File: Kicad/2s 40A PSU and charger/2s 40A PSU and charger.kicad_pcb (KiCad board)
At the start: 4 copper layers, 45 x 20 mm, 109 parts, among them J1 Keystone 3579, J10 USB_C_Receptacle_USB2.0_16P, J11 1.27mm 4 pin socket, J12 USB, J2 JST XH-S Balance Plug, J3 Keystone 3579, J4 Keystone 3569, J5 Keystone 3569, J6 Keystone 3579, J7 Keystone 3579, J8 Keystone 3569, J9 Keystone 3569, Q1 PJA3430, Q2 PJA3430, Q3 Vishay sir404dp, or SiR500DP, Q4 PJA3430, Q5 PJA3430, Q6 Vishay sir404dp, or SiR500DP, U1 BQ76905RGRR, U2 AP63203WU, U3 BQ24780SRUYR, U5 THVD1420DRLR, U6 CH32X035G8U6, U7 TPS7A2633DRV

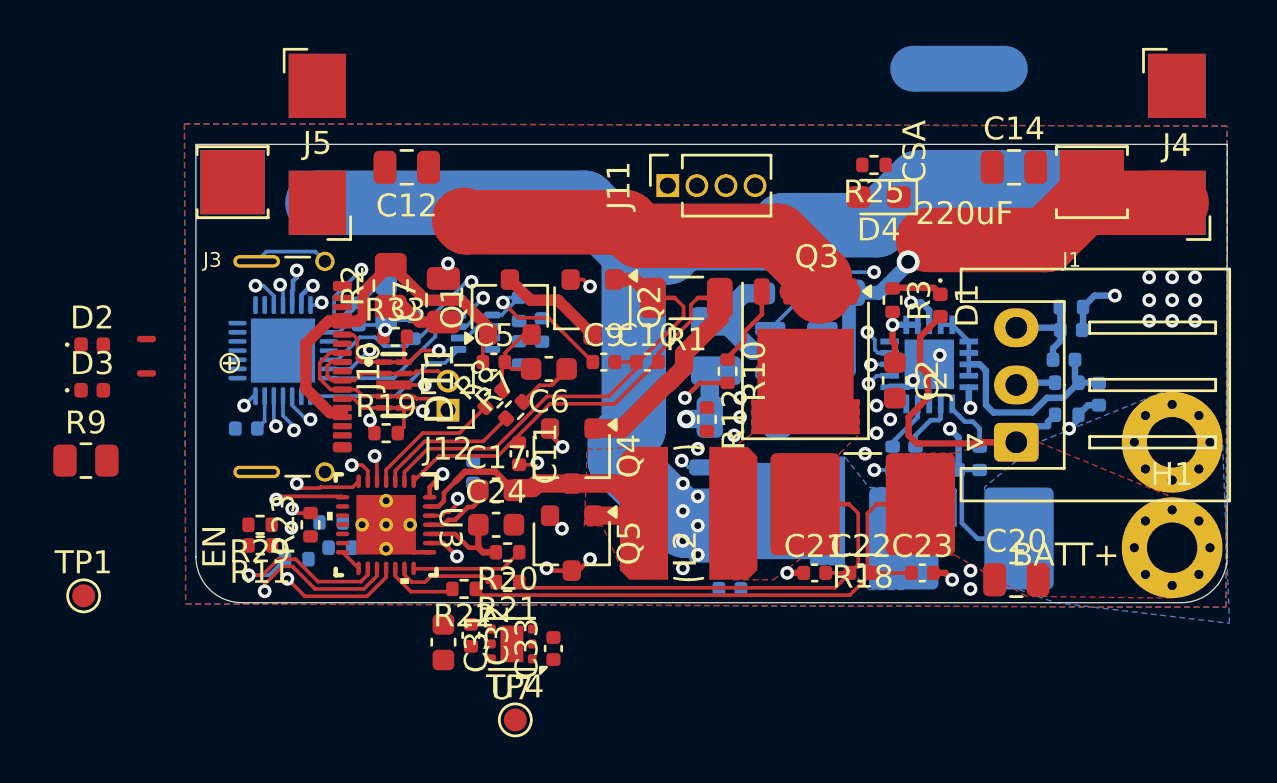
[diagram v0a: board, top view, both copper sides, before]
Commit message: Finished Layout of PSU
Gosh, this has taken a long time on and off, almost 2 months!
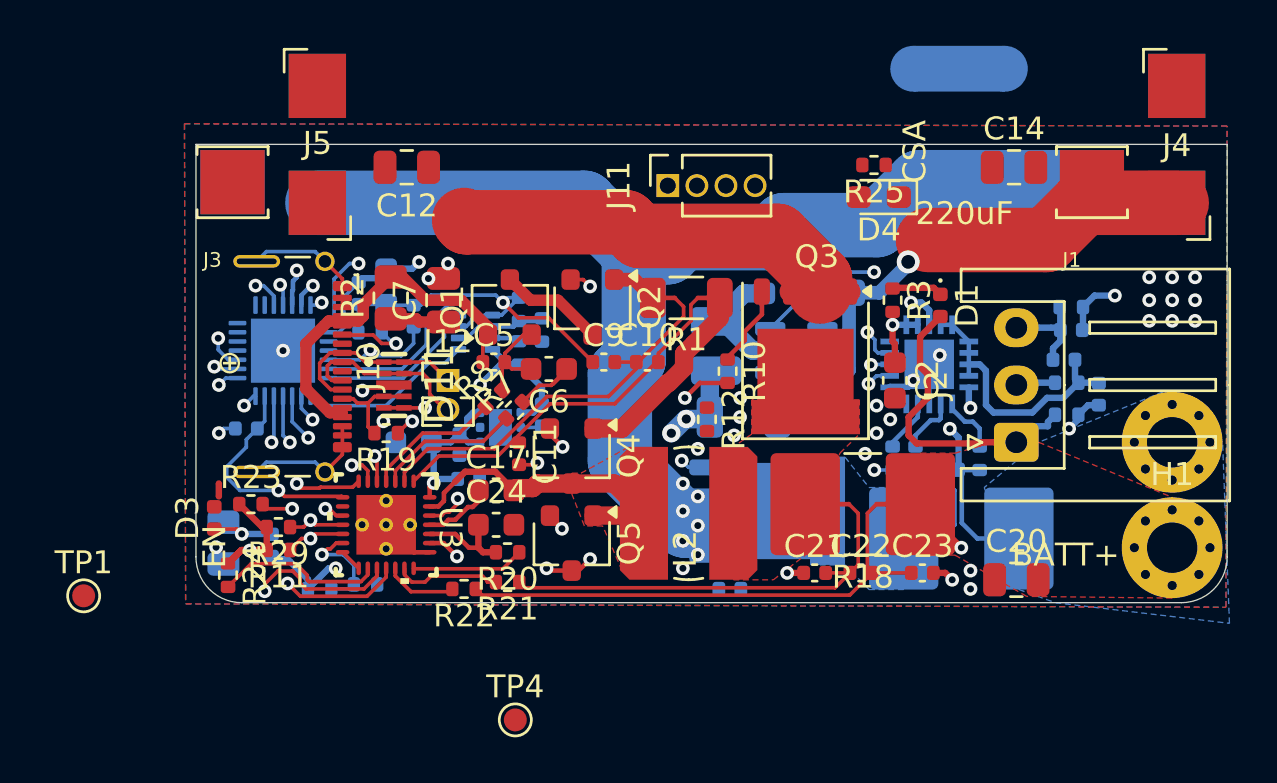
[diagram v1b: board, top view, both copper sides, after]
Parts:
- C31, C32, C33, D2, NT10, R33, R9, U7: moved to B.Cu
- J10: value USB_C_Receptacle_USB2.0_16P -> G-Switch-GT-USB-7025
- R24: moved to F.Cu
- moved NT10 11.8 mm to (112.4, 130.4), turned to -45 degrees
- moved D2 11.7 mm to (111.4, 129.5), turned to -90 degrees
- moved C33 10.2 mm to (123.2, 123.8), turned to -90 degrees
- moved U7 9.46 mm to (121.4, 124.3)
- moved C31 8.82 mm to (117.6, 125.0), turned to 180 degrees
- moved C32 8.34 mm to (119.6, 125.1)
- moved D3 7.71 mm to (108.9, 128.3), turned to 90 degrees
- moved R9 7.00 mm to (109.3, 129.4), turned to 90 degrees
- moved NT12 5.99 mm to (109.1, 127.1), turned to 90 degrees
- moved R24 3.08 mm to (109.5, 130.8), turned to -90 degrees
- moved R30 2.94 mm to (113.5, 131.4)
- moved R23 2.75 mm to (110.5, 127.7), turned to 0 degrees
- moved R31 1.94 mm to (115.5, 131.2)
- moved J12 1.30 mm to (119.1, 122.3), turned to 0 degrees
- moved R33 1.12 mm to (115.7, 120.2)
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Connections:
- D11 pad 1: /Connectors/CC1 -> /Connectors/D+
- D11 pad 10: /Connectors/CC1 -> /Connectors/D+
- D11 pad 4: /Connectors/D+ -> /Connectors/CC2
- D11 pad 5: /Connectors/CC2 -> /Connectors/CC1
- D11 pad 6: /Connectors/CC2 -> /Connectors/CC1
- D11 pad 7: /Connectors/D+ -> /Connectors/CC2
- NT12 pad 2: /Battery Charger/MOTORPWR -> /Battery Charger/IN
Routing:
- net GND: track 19.6 -> 35.5 mm, vias 7 -> 8
- net /Battery Charger/MCU3.3v: track 3.64 -> 18.4 mm, vias 0 -> 3
- net /Battery Charger/Always On PWR: track 1.25 -> 8.40 mm, vias 1 -> 2
- net /Battery Balancer/+BAT: track 0.00 -> 5.19 mm, vias 0 -> 2
- net /MCU/UART1-RTS: track 4.03 -> 9.21 mm, vias 2 -> 0
- net /Battery Charger/Charger IDCHG: track 4.52 -> 9.64 mm
- net Net-(U3-CMPIN): track 0.00 -> 4.58 mm, vias 0 -> 1
- net /Battery Charger/Charger IADP: track 11.1 -> 7.84 mm
- net Net-(D2-K): track 0.00 -> 2.60 mm, vias 0 -> 1
- net /SCL: track 2.45 -> 5.03 mm, vias 2 -> 3
- net /SDA: track 1.77 -> 4.26 mm, vias 2 -> 3
- net /Connectors/RS485-: track 0.00 -> 2.31 mm
- net /Connectors/RS485+: track 0.00 -> 2.23 mm
- net /Connectors/3.3v: track 8.03 -> 9.88 mm, vias 2 -> 3
- net /Battery Charger/Charger PROCHOT: track 0.00 -> 1.82 mm, vias 0 -> 2
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
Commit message: Updated 3v3 psu traces and capacitor position
I rotated the input capacitor to make a more compact shape, and I played around with some of the trace thicknesses
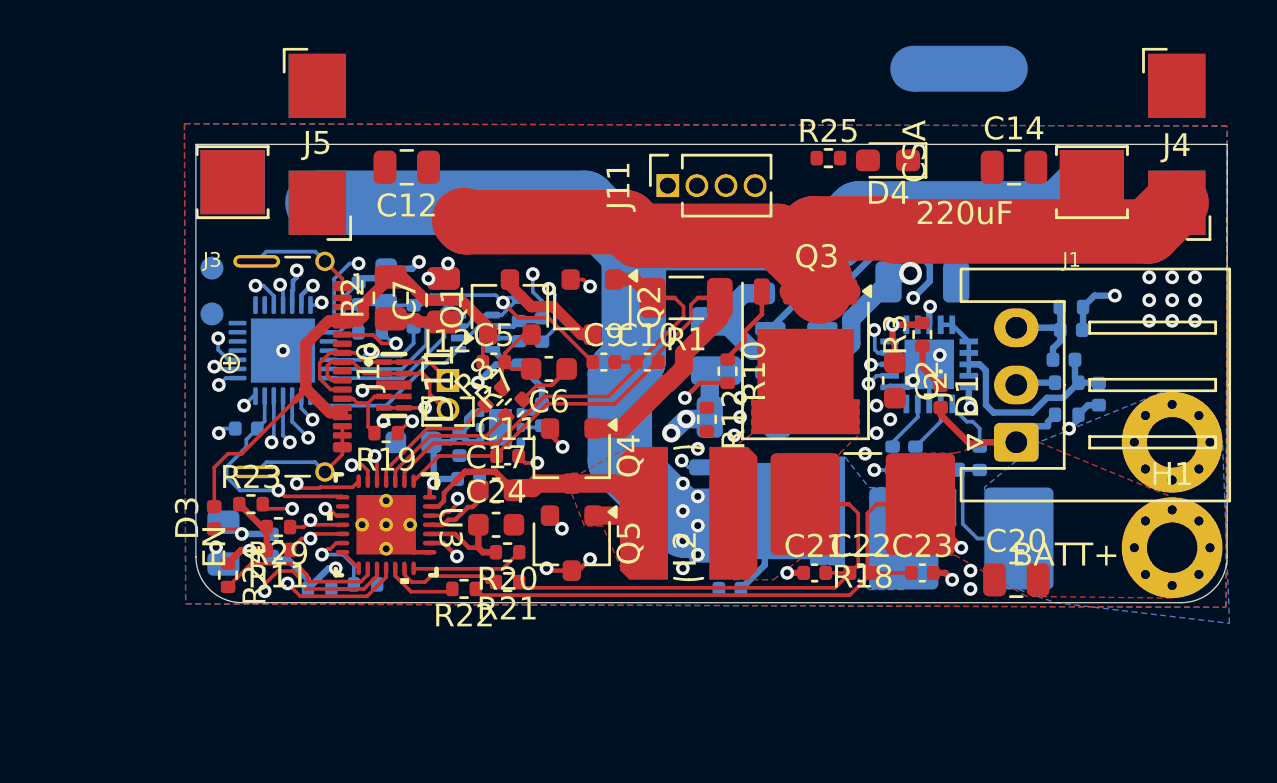
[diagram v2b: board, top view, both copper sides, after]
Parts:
- TP1, TP4: moved to B.Cu
- moved TP4 23.7 mm to (108.8, 117.4), turned to 180 degrees
- moved TP1 13.5 mm to (108.8, 119.4), turned to 180 degrees
- moved NT12 5.38 mm to (112.6, 123.0), turned to 45 degrees
- moved D1 3.97 mm to (140.6, 123.0)
- moved C28 3.54 mm to (139.8, 118.0), turned to 0 degrees
- moved R25 2.01 mm to (135.7, 112.6), turned to 0 degrees
- moved R3 1.98 mm to (139.8, 120.3), turned to 90 degrees
- moved D4 1.65 mm to (138.3, 112.7)
- moved C11 0.51 mm to (121.7, 125.6), turned to 0 degrees
- moved R7 0.10 mm to (122.0, 123.5)
- moved R8 0.10 mm to (121.1, 123.0)
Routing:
- net /Battery Charger/MOTORPWR: track 40.6 -> 50.0 mm
- net Net-(D1-A): track 9.37 -> 2.62 mm
- net Net-(D3-A): track 0.00 -> 6.42 mm
- net Net-(Q6-S): track 5.99 -> 9.82 mm
- net /Connectors/3.3v: track 9.88 -> 13.6 mm
- net Net-(Q1-G): track 8.82 -> 5.32 mm
- net /Connectors/RS485+: track 2.23 -> 4.88 mm, vias 0 -> 1
- net /Connectors/RS485-: track 2.31 -> 4.40 mm, vias 0 -> 1
- net /Battery Balancer/-BAT: track 29.5 -> 27.5 mm, vias 3 -> 2
- net /Battery Balancer/Up: track 17.6 -> 16.2 mm
- net Net-(U1-BAT): track 3.36 -> 4.13 mm

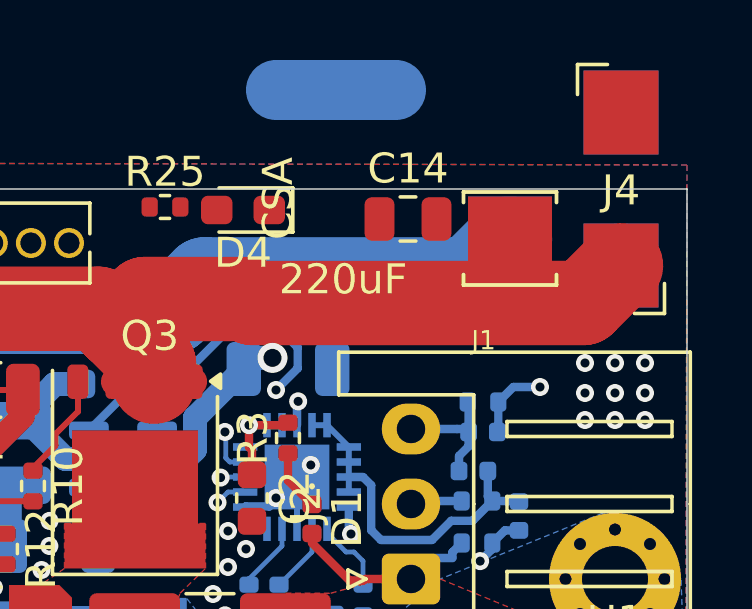
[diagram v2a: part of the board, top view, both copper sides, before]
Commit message: Combined separate ground planes
I now have one solid ground plane. There really was no point in having separate ground planes EXCEPT for keeping the high current return path away from the MCU and sense lines. I have added a keepout zone on the top half, to split to keep the high current return from going into the MCU section, but that is it.
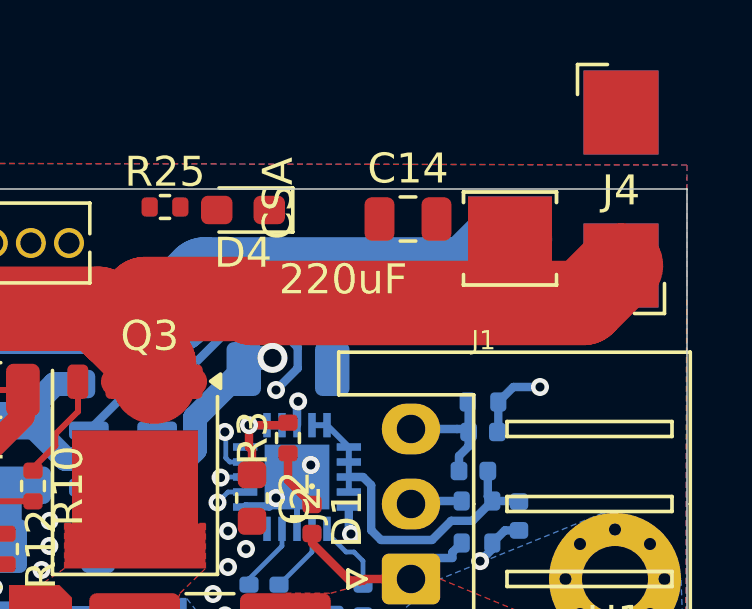
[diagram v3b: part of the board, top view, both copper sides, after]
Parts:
- removed NT1: Main GND NetTie, NetTie:NetTie-2_SMD_Pad2.0mm
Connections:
- C12 pad 1: GNDPWR -> GND
- C14 pad 1: GNDPWR -> GND
- C2 pad 2: GNDPWR -> /Battery Balancer/-BAT
- C20 pad 1: GNDPWR -> GND
- C24 pad 2: GNDPWR -> GND
- C28 pad 2: GNDPWR -> GND
- C31 pad 2: GNDPWR -> GND
- C32 pad 2: GNDPWR -> GND
- C4 pad 2: GNDPWR -> GND
- C7 pad 2: GNDPWR -> GND
- J6 pad 1: GNDPWR -> GND
- J7 pad 1: GNDPWR -> GND
- J8 pad 1: GNDPWR -> GND
- J9 pad 1: GNDPWR -> GND
- Q5 pad 3: GNDPWR -> GND
- Q6 pad 1: GNDPWR -> GND
- Q6 pad 2: GNDPWR -> GND
- Q6 pad 3: GNDPWR -> GND
- R31 pad 1: GNDPWR -> GND
- U2 pad 4: GNDPWR -> GND
- U3 pad 22: GNDPWR -> GND
- U3 pad 29: GNDPWR -> GND
- U7 pad 5: GNDPWR -> GND
- U7 pad 7: GNDPWR -> GND
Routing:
- net GNDPWR: track 55.3 -> 0.00 mm, vias 29 -> 0
- net GND: track 35.6 -> 90.9 mm, vias 8 -> 28
- added copper zone on B.Cu, net GND
- added copper zone on F.Cu, net GND
- added copper zone on In1.Cu, net GND
- added copper zone on In2.Cu, net GND
- removed copper zone on B.Cu, net GNDPWR
- removed copper zone on F.Cu, net GNDPWR
- removed copper zone on In1.Cu, net GNDPWR
- removed copper zone on In2.Cu, net GNDPWR

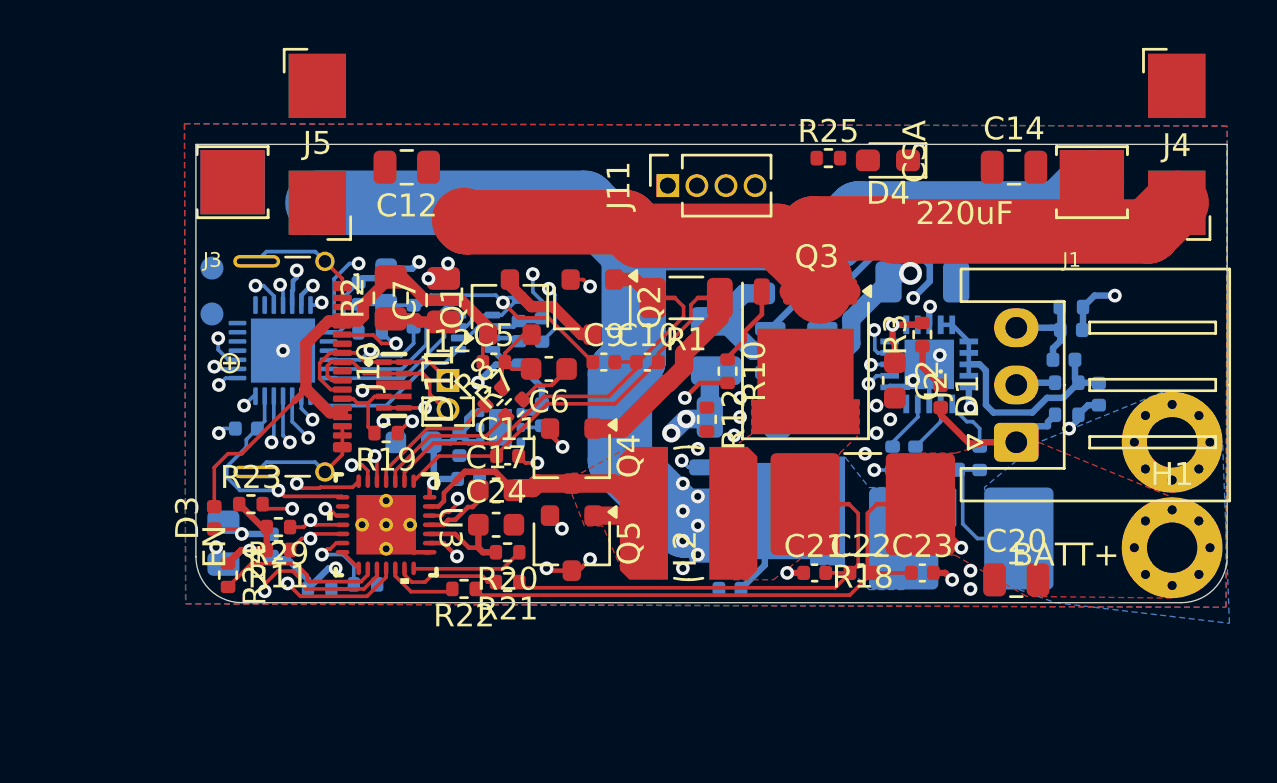
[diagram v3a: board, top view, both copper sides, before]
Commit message: Finished routing PSU
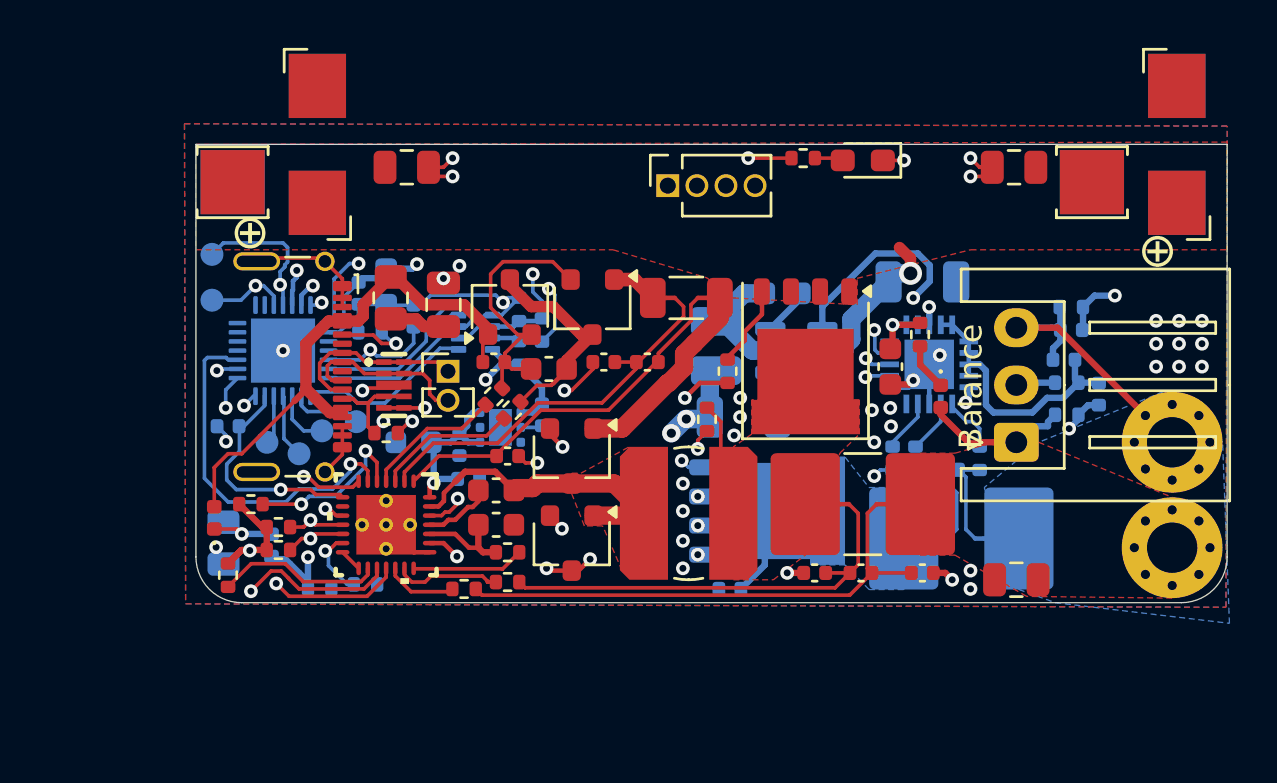
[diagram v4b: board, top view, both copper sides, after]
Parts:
- added NT1: Sense NetTie, custom_Connector:NetTie-2_SMD_Pad0.2mm, B.Cu at (142.3, 129.2)
- added NT11: Sense NetTie, custom_Connector:NetTie-2_SMD_Pad0.2mm, B.Cu at (140.7, 129.2)
- added TP2: CS, TestPoint:TestPoint_Pad_D1.0mm, B.Cu at (115.1, 124.1)
- added TP3: SCK, TestPoint:TestPoint_Pad_D1.0mm, B.Cu at (113.6, 124.5)
- added TP5: SDI, TestPoint:TestPoint_Pad_D1.0mm, B.Cu at (112.6, 125.5)
- added TP6: SDO, TestPoint:TestPoint_Pad_D1.0mm, B.Cu at (111.2, 125.0)
- J10: footprint Connector_USB:USB_C_Receptacle_G-Switch_GT-USB-7025 -> custom_Connector:USB_C_G-Switch_GT-USB-7025-JLCPCBv
- moved D4 1.10 mm to (137.2, 112.7)
- moved R25 1.10 mm to (134.6, 112.6)
- moved C30 0.81 mm to (109.5, 124.3)
- moved C2 0.63 mm to (138.4, 121.7)
- moved TP1 0.60 mm to (108.8, 118.8)
- moved TP4 0.60 mm to (108.8, 116.8)
- moved J12 0.40 mm to (119.1, 121.9)
- moved C7 0.20 mm to (118.9, 119.0)
- moved R7 0.14 mm to (121.9, 123.6)
- moved R3 0.10 mm to (139.7, 120.3)
- moved NT10 0.10 mm to (112.4, 130.5)
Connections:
- C3 pad 1: /Battery Balancer/-BAT -> Net-(C3-Pad1)
- C3 pad 2: Net-(Q6-S) -> Net-(C3-Pad2)
- R4 pad 2: /Battery Balancer/-BAT -> Net-(C3-Pad1)
- R5 pad 2: Net-(Q6-S) -> Net-(C3-Pad2)
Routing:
- net /Connectors/3.3v: track 13.6 -> 63.6 mm
- net /SDA: track 4.26 -> 51.7 mm
- net /SCL: track 5.03 -> 49.8 mm
- net GND: track 90.9 -> 48.1 mm, vias 28 -> 43
- net /Battery Charger/MOTORPWR: track 50.0 -> 8.54 mm
- net /Battery Balancer/+BAT: track 5.19 -> 39.8 mm, vias 2 -> 1
- net /Battery Balancer/Balancer Alert: track 2.25 -> 35.3 mm
- net /MCU/LED: track 1.05 -> 32.5 mm, vias 1 -> 2
- net /Battery Charger/MCU3.3v: track 18.5 -> 43.8 mm
- net /Connectors/CC1: track 5.65 -> 21.8 mm
- net /Connectors/RS485-: track 4.40 -> 18.6 mm
- net /Connectors/CC2: track 8.36 -> 22.3 mm
- net /Connectors/RS485+: track 4.88 -> 18.5 mm
- net /Battery Charger/Always On PWR: track 8.40 -> 21.9 mm
- net /Connectors/D+: track 9.25 -> 22.7 mm
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- added copper zone on F.Cu, net /Battery Charger/MOTORPWR
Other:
- board text added: "+ D+D- -"
- board text added: "BAT+"
- board text added: "BAT-"
- board text added: "Balance"
- board text added: "SWC , SWD"
- board text added: "©2024 Asher Edwards"
- board text removed: "220uF"
- board text removed: "BATT+"
- board text removed: "BATT-"
- board text removed: "CSA"
- board text removed: "EN"
- board text removed: "© 2024 Asher Edwards"
